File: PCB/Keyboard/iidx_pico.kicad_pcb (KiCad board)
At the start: 2 copper layers, 180 x 160 mm, 77 parts, among them J1 CONN_01x05, J2 CONN_01x05, J3 PJ393-8P, SW1 SWITCH_SPST, SW10 SWITCH_SPST, SW11 SWITCH_SPST, SW12 Tact_4pin, SW13 Tact_4pin, SW2 SWITCH_SPST, SW3 SWITCH_SPST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

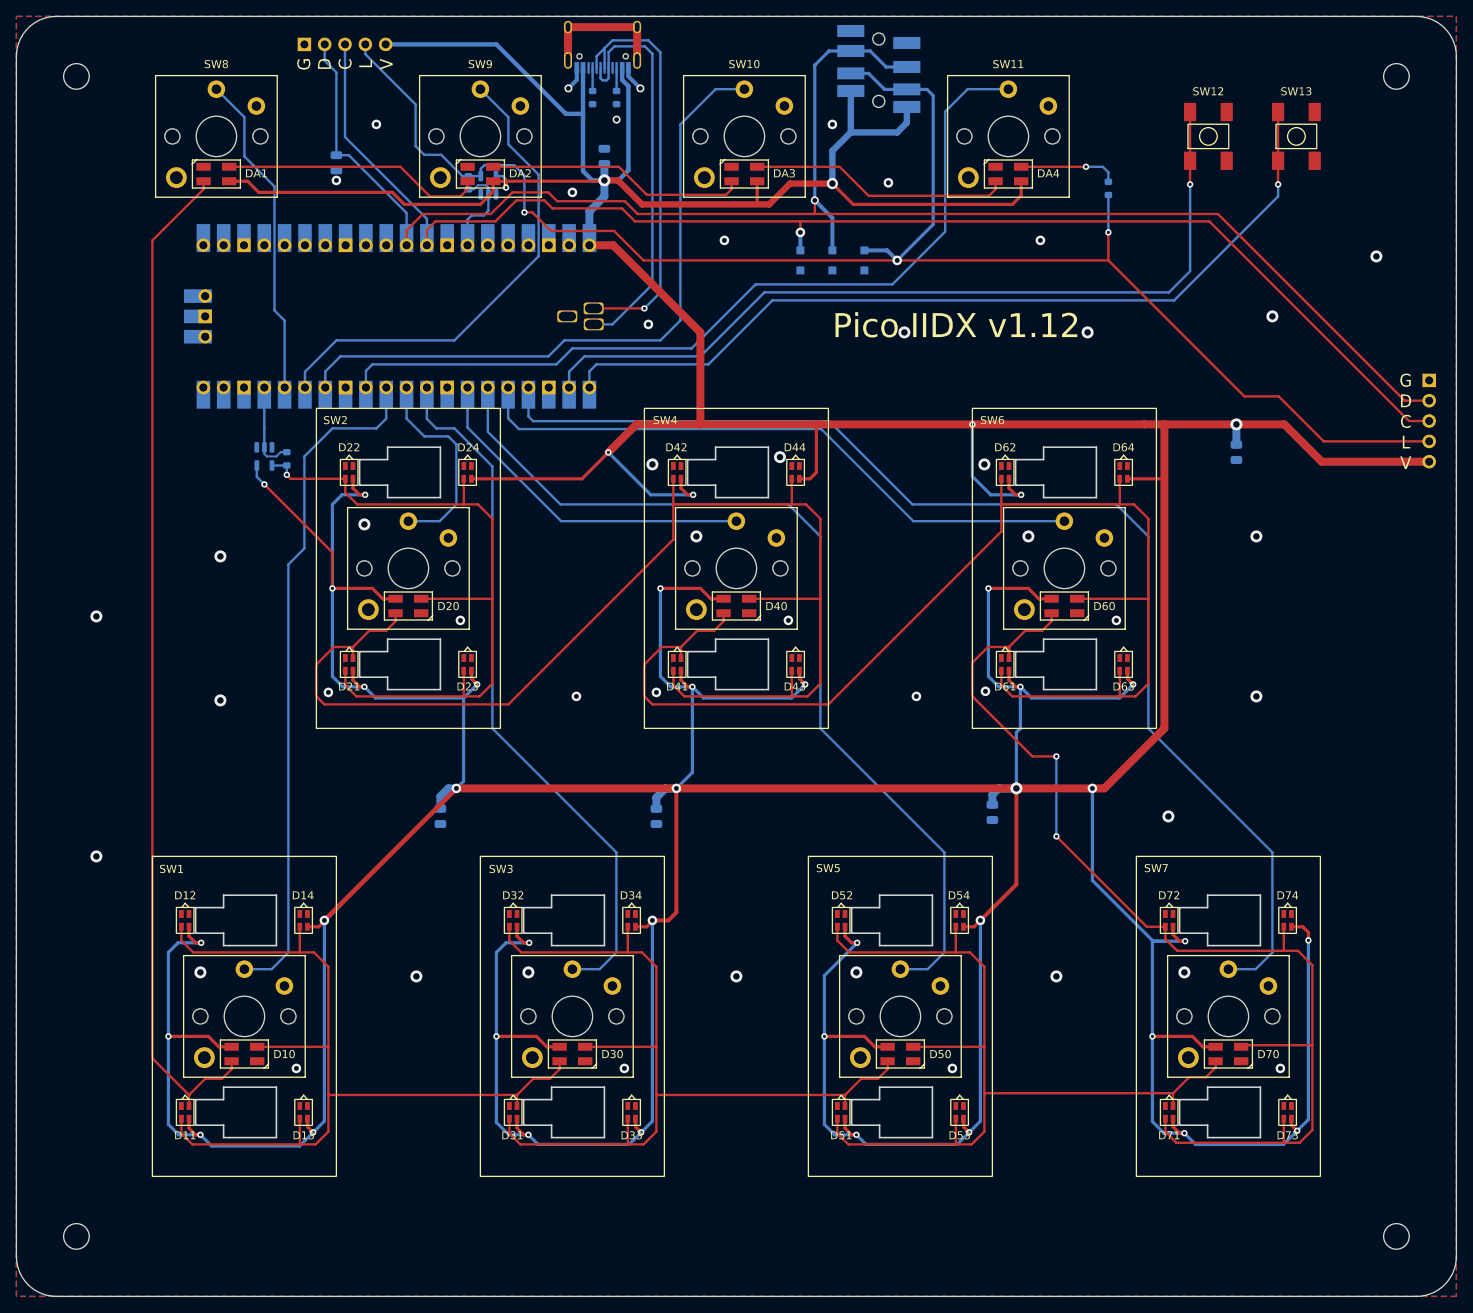
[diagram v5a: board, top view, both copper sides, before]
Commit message: Removal of confusion parts in PCB
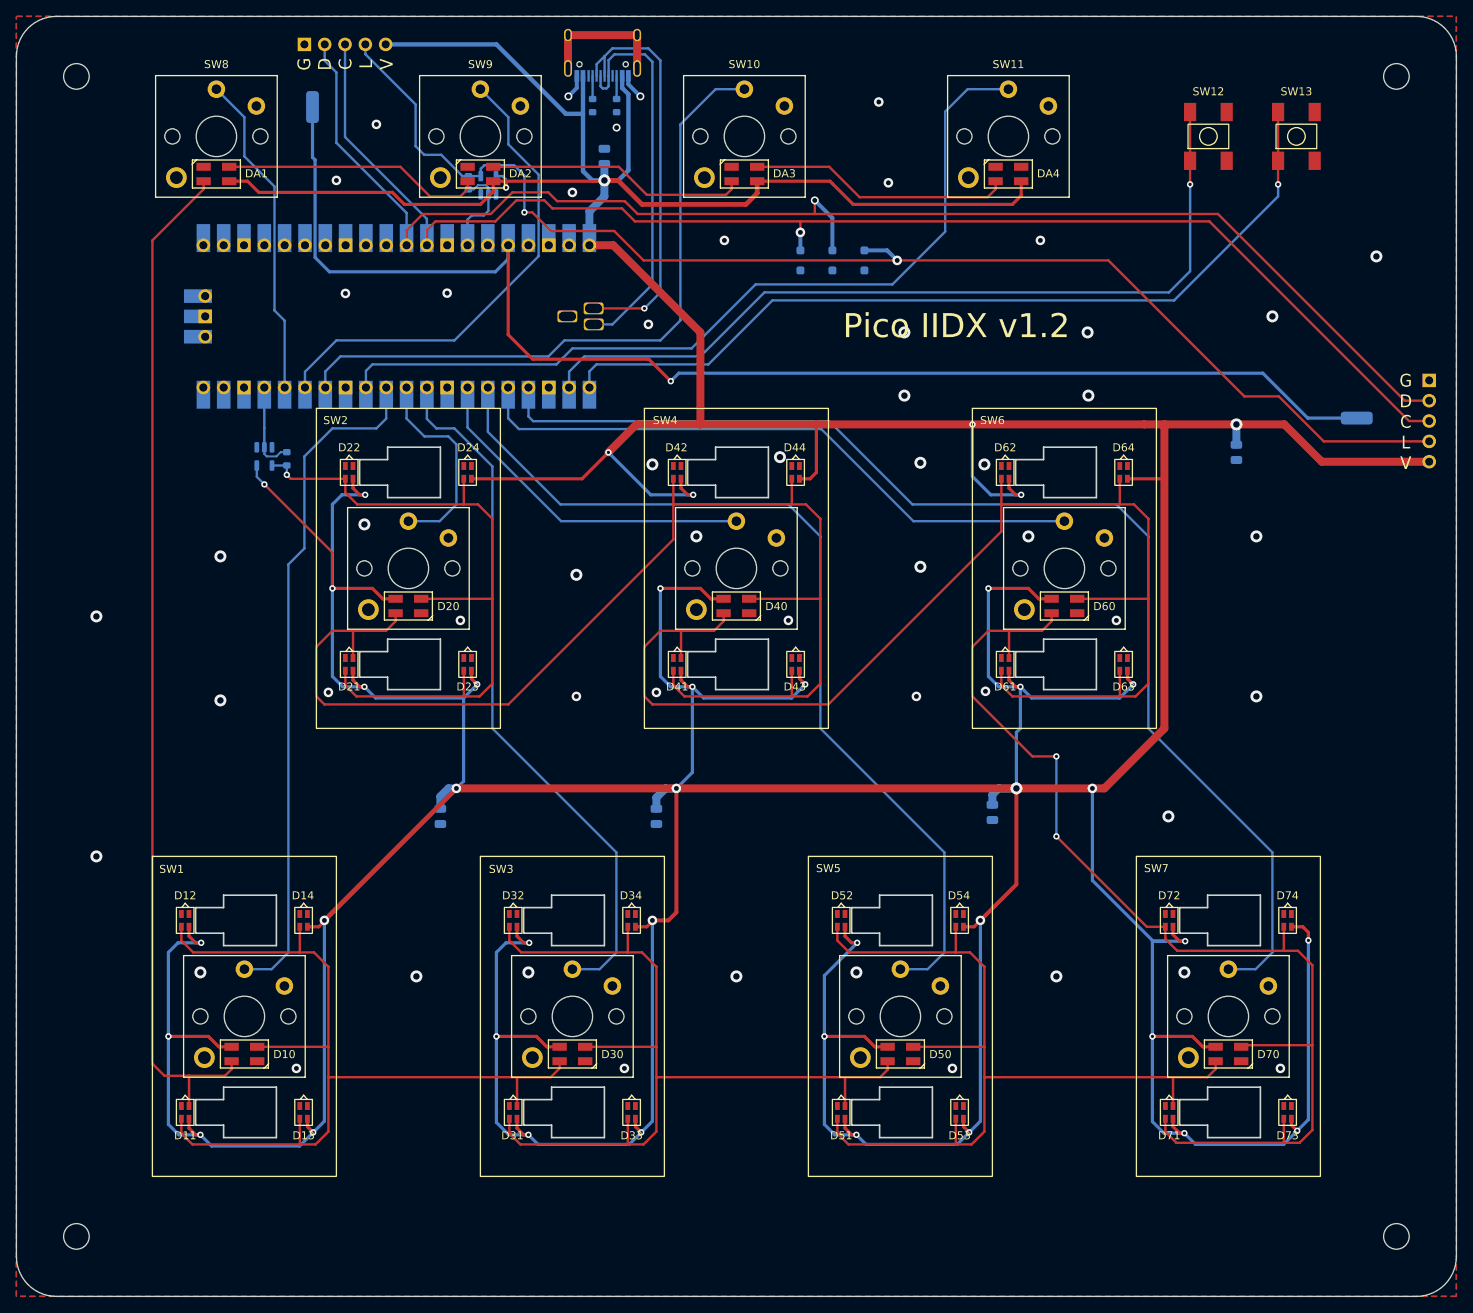
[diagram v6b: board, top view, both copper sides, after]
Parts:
- removed C6: 1nF, Capacitor_SMD:C_0805_2012Metric
- removed the R1 at (183.8, 40.9)
- added J4: Conn_01x01, iidx_pico:Solder_1P, B.Cu at (214.9, 69.6)
- J3: value PJ393-8P -> Conn_01x01; footprint iidx_pico:PJ393-8P -> iidx_pico:Solder_1P
- moved J3 70.9 mm to (84.3, 30.7), turned to 90 degrees
- moved R20 1.00 mm to (119.3, 30.6)
- moved R21 1.00 mm to (122.3, 30.6)
- moved USB1 1.00 mm to (120.6, 19.1)
- renumbered R2 to R1, R3 to R2
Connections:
- DA4 pad O: Net-(DA4-PadO) -> unconnected-(DA4-Out-PadO)
- U1 pad 36: unconnected-(U1-Pad36) -> +3.3V
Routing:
- net +3.3V: track 0.00 -> 168.6 mm, vias 0 -> 1
- net /TT_LED: track 208.4 -> 166.3 mm, vias 3 -> 2
- net /SDA: track 211.5 -> 180.7 mm
- net +5V: track 1210.3 -> 1184.5 mm, vias 43 -> 42
- net Net-(DA4-PadO): track 12.4 -> 0.00 mm, vias 1 -> 0
- net /LED6: track 155.4 -> 158.7 mm
- net /LED4: track 156.0 -> 159.3 mm
- net /LED7: track 139.2 -> 142.4 mm
- net /LED5: track 111.3 -> 112.8 mm
- net /LED3: track 111.3 -> 112.6 mm
- net /LED1: track 111.3 -> 112.5 mm
- net Net-(USB1-DN1): track 52.5 -> 51.5 mm
- net Net-(USB1-DP1): track 50.2 -> 49.2 mm
- net /LED8: track 127.8 -> 128.6 mm
- net GND: vias 47 -> 54
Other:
- board text added: "Pico IIDX v1.2"
- board text removed: "Pico IIDX v1.12"

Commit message: PCB v1.3 fixes key "sticky-feel" problem
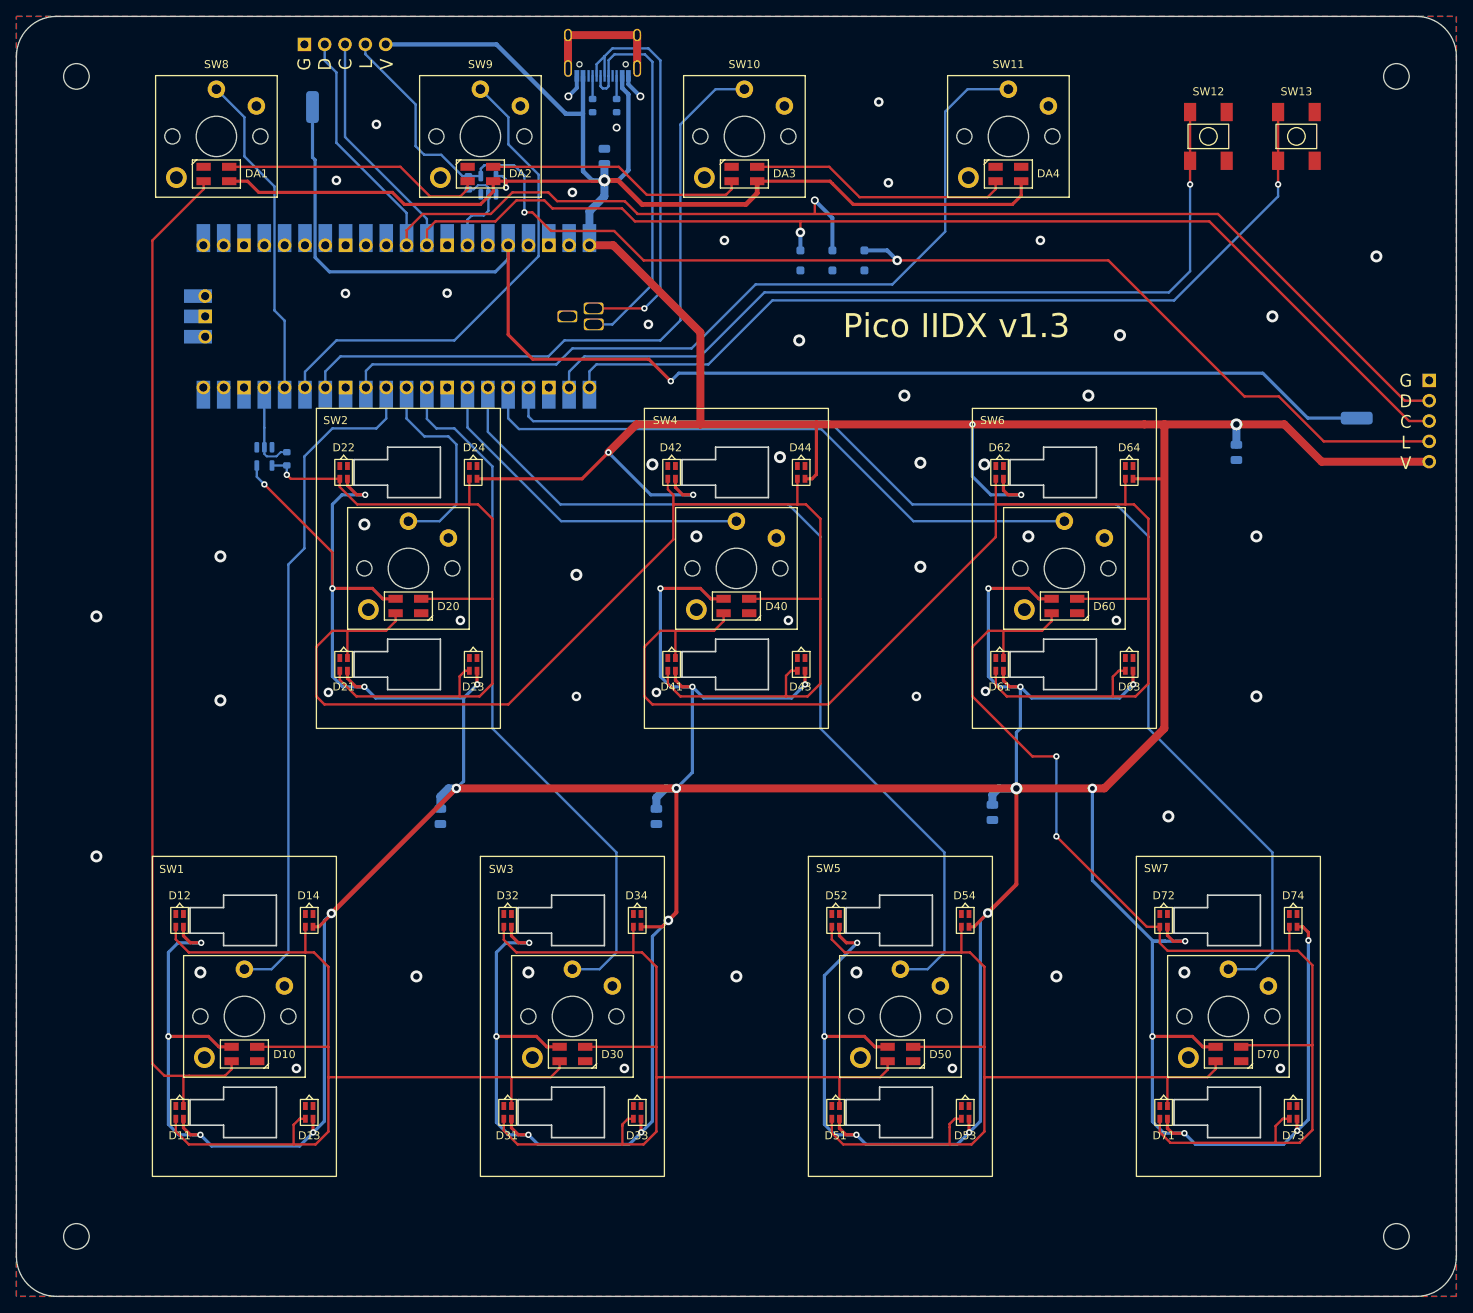
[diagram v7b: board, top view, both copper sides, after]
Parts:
- moved D11 0.70 mm to (67.7, 156.4)
- moved D12 0.70 mm to (67.7, 132.4)
- moved D13 0.70 mm to (83.9, 156.4)
- moved D14 0.70 mm to (83.9, 132.4)
- moved D21 0.70 mm to (88.2, 100.4)
- moved D22 0.70 mm to (88.2, 76.4)
- moved D23 0.70 mm to (104.4, 100.4)
- moved D24 0.70 mm to (104.4, 76.4)
- moved D31 0.70 mm to (108.7, 156.4)
- moved D32 0.70 mm to (108.7, 132.4)
- moved D33 0.70 mm to (124.9, 156.4)
- moved D34 0.70 mm to (124.9, 132.4)
- moved D41 0.70 mm to (129.2, 100.4)
- moved D42 0.70 mm to (129.2, 76.4)
- moved D43 0.70 mm to (145.4, 100.4)
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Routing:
- net +5V: track 1184.5 -> 1190.2 mm
- net /LED5: track 112.8 -> 115.3 mm
- net /LED6: track 158.7 -> 161.1 mm
- net /LED1: track 112.5 -> 114.8 mm
- net /LED3: track 112.6 -> 114.8 mm
- net /LED4: track 159.3 -> 161.4 mm
- net /LED7: track 142.4 -> 143.9 mm
- net /LED2: track 89.2 -> 90.0 mm
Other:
- board text added: "Pico IIDX v1.3"
- board text removed: "Pico IIDX v1.2"

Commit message: PCB v1.4 (sensor on board)
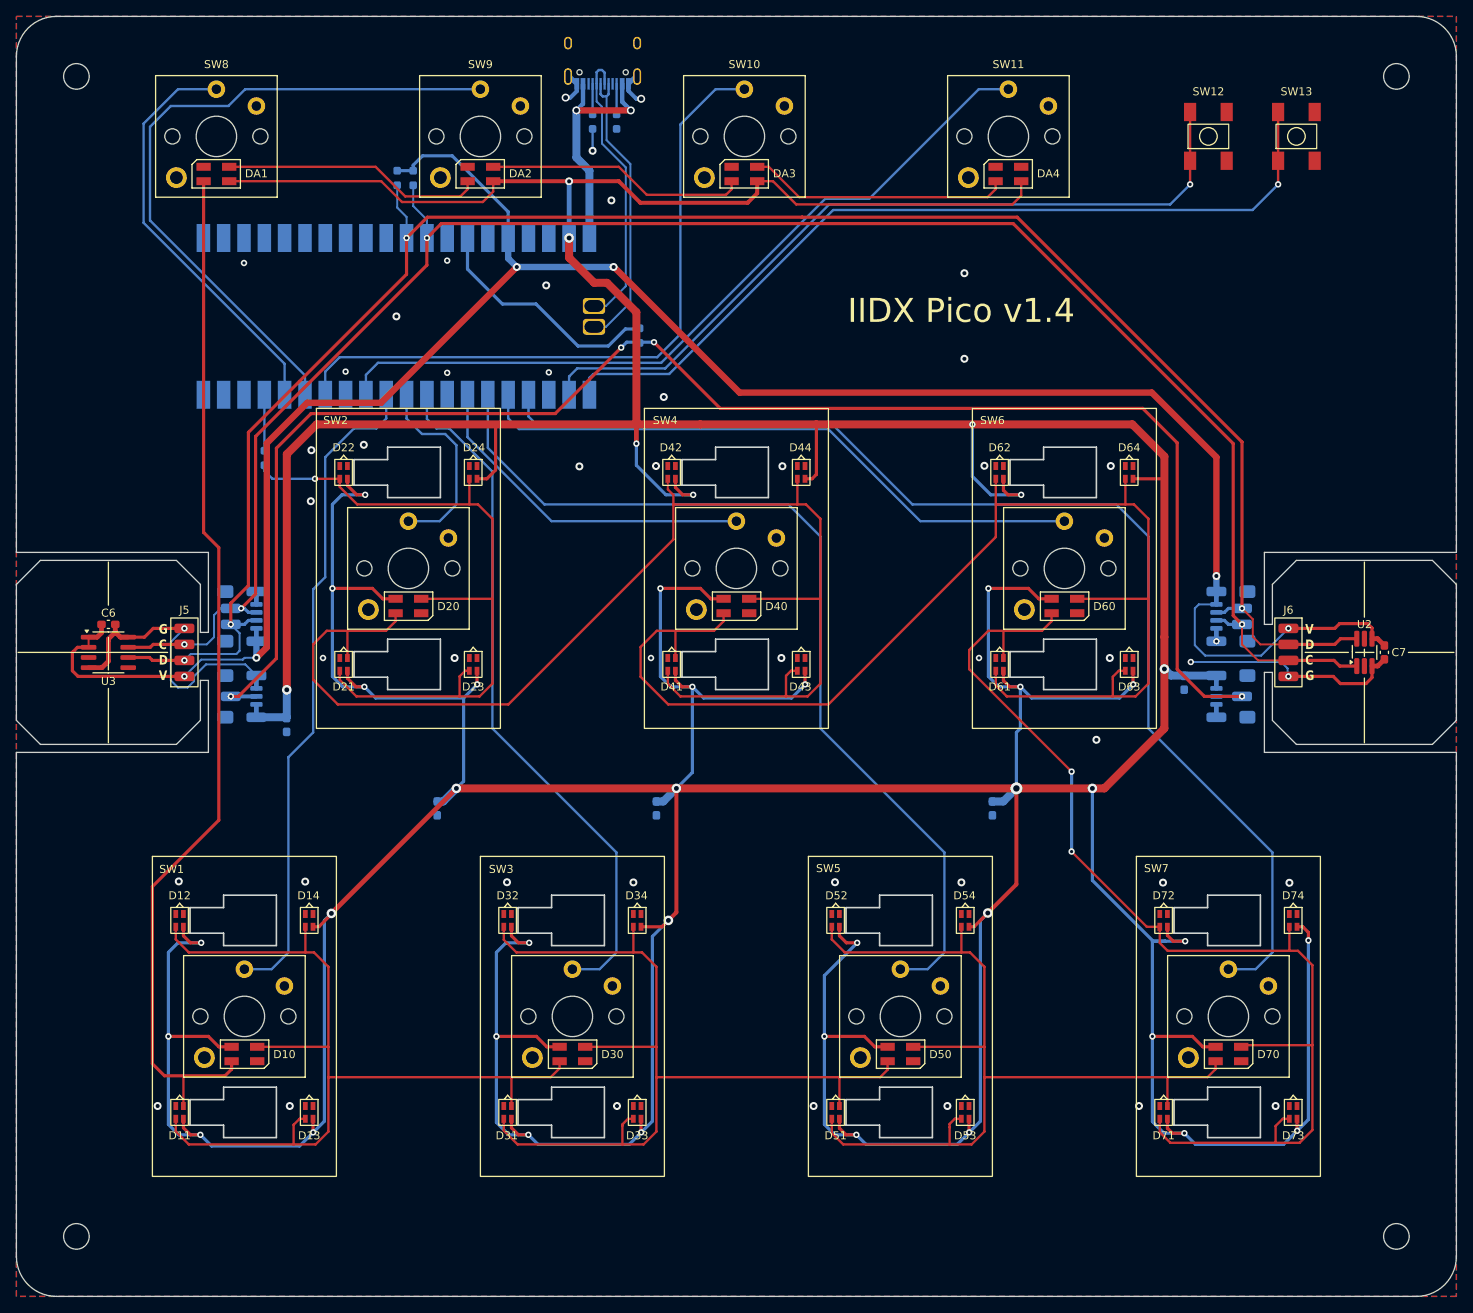
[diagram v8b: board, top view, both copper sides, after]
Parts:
- removed TV1, TV2, TV3: D_TVS, Diode_SMD:D_SOD-323_HandSoldering
- added C6: 1uF, Capacitor_SMD:C_0603_1608Metric_Pad1.08x0.95mm_HandSolder, F.Cu at (58.8, 95.4)
- added C7: 1uF, Capacitor_SMD:C_0603_1608Metric_Pad1.08x0.95mm_HandSolder, F.Cu at (218.3, 98.9)
- added J5: Spin, iidx_pico:P2.0_4P_Solder, F.Cu at (68.3, 98.9)
- added J6: Spin, iidx_pico:P2.0_4P_Solder, F.Cu at (206.3, 98.9)
- added R3: 4.7K, Resistor_SMD:R_0603_1608Metric_Pad0.98x0.95mm_HandSolder, B.Cu at (96.9, 39.6)
- added R4: 4.7K, Resistor_SMD:R_0603_1608Metric_Pad0.98x0.95mm_HandSolder, B.Cu at (94.9, 39.6)
- C1, C2, C3, C4, C5: footprint Capacitor_SMD:C_0805_2012Metric -> Capacitor_SMD:C_0603_1608Metric_Pad1.08x0.95mm_HandSolder
- J1, J2: value CONN_01x05 -> Spin; footprint iidx_pico:Pogo_5P_Female -> iidx_pico:SH1.0_4P_Solder_Combo
- J3, J4: value Conn_01x01 -> RGB; footprint iidx_pico:Solder_1P -> iidx_pico:SH1.0_3P_Solder_Combo
- R1, R2, R20, R21: footprint Resistor_SMD:R_0603_1608Metric -> Resistor_SMD:R_0603_1608Metric_Pad0.98x0.95mm_HandSolder
- U1: value Pico -> PiPico_No_SWD; footprint MCU_RaspberryPi_and_Boards:RPi_Pico_SMD -> iidx_pico:RPi_Pico_SMD_Pins_No_SWD
- U2: value SN74LV1T34DBV -> TMAG5273; footprint iidx_pico:SOT-23-5_Jumper -> Package_TO_SOT_SMD:TSOT-23-6_HandSoldering; moved to F.Cu
- U3: value SN74LV1T34DBV -> AS5600; footprint iidx_pico:SOT-23-5_Jumper -> Package_SO:SOIC-8_3.9x4.9mm_P1.27mm; moved to F.Cu
- moved U2 139.7 mm to (215.8, 98.9), turned to 90 degrees
- moved C1 81.4 mm to (81.1, 108.0), turned to -90 degrees
- moved U3 75.3 mm to (58.8, 98.9), turned to 0 degrees
- moved J3 74.2 mm to (75.3, 104.4)
- moved J1 71.9 mm to (75.3, 94.4), turned to 90 degrees
- moved J2 38.4 mm to (199.3, 94.4), turned to -90 degrees
- moved J4 38.1 mm to (199.3, 104.4), turned to -90 degrees
- moved C2 29.5 mm to (193.3, 102.7)
- moved R2 28.7 mm to (125.2, 59.3), turned to 90 degrees
- moved R1 2.80 mm to (78.3, 74.6)
- moved R20 2.00 mm to (119.3, 32.5)
- moved R21 2.00 mm to (122.3, 32.5)
- moved C5 1.08 mm to (99.9, 118.4)
- moved C4 1.00 mm to (127.3, 118.4)
- moved USB1 1.00 mm to (120.6, 20.1)
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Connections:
- J1 pad 1: GND -> +3.3V
- J1 pad 4: /TT_LED -> GND
- J2 pad 1: GND -> +3.3V
- J2 pad 4: /TT_LED -> GND
- J3 pad 1: +3.3V -> +5V
- J4 pad 1: +3.3V -> +5V
- U1 pad 39: unconnected-(U1-VSYS-Pad39) -> +5V
- U1 pad 40: +5V -> VBUS
- U2 pad 1: unconnected-(U2-NC-Pad1) -> /SCL
- U2 pad 2: Net-(U1-GPIO13) -> GND
- U2 pad 4: /LED2 -> +3.3V
- U2 pad 5: +5V -> unconnected-(U2-~{INT}-Pad5)
- U3 pad 1: unconnected-(U3-NC-Pad1) -> +3.3V
- U3 pad 2: Net-(U1-GPIO28_ADC2) -> +3.3V
- U3 pad 3: GND -> unconnected-(U3-OUT-Pad3)
- U3 pad 4: /TT_LED -> GND
- U3 pad 5: +5V -> unconnected-(U3-PGO-Pad5)
- USB1 pad 11: +5V -> VBUS
- USB1 pad 13: unconnected-(USB1-SHIELD-Pad13) -> GND
- USB1 pad 2: +5V -> VBUS
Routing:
- net +3.3V: track 168.6 -> 280.9 mm, vias 1 -> 6
- net GND: track 6.19 -> 83.1 mm, vias 54 -> 48
- net /SCL: track 173.1 -> 240.4 mm, vias 1 -> 4
- net /SDA: track 180.7 -> 245.4 mm, vias 1 -> 4
- net +5V: track 1190.2 -> 1137.9 mm
- net /TT_LED: track 166.3 -> 201.4 mm, vias 2 -> 4
- net VBUS: track 0.00 -> 31.8 mm, vias 0 -> 2
- net Net-(U1-GPIO11): track 61.0 -> 84.8 mm
- net Net-(U1-GPIO28_ADC2): track 11.8 -> 30.3 mm
- net unconnected-(USB1-SHIELD-Pad13): track 17.0 -> 0.00 mm
- net Net-(U1-USB1): track 51.5 -> 35.9 mm, vias 1 -> 0
- net Net-(U1-USB2): track 49.2 -> 36.6 mm
- net Net-(U1-GPIO12): track 40.8 -> 52.1 mm
- net Net-(U1-GPIO9): track 105.8 -> 96.7 mm
- net Net-(U1-GPIO1): track 104.7 -> 98.0 mm
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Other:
- outline, holes or cut-outs redrawn
- board text added: "G C D V"
- board text added: "G L V"
- board text added: "IIDX Pico v1.4"
- board text added: "V D C G"
- board text added: "V L G"
- board text removed: "G D C L V"
- board text removed: "Pico IIDX v1.3"
